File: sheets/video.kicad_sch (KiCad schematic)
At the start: 29 parts, among them U10 74LS273, U11 74LS05, U5 NEO-G0, U6 4364, U7 4364, U80 74HC04, U9 74LS273

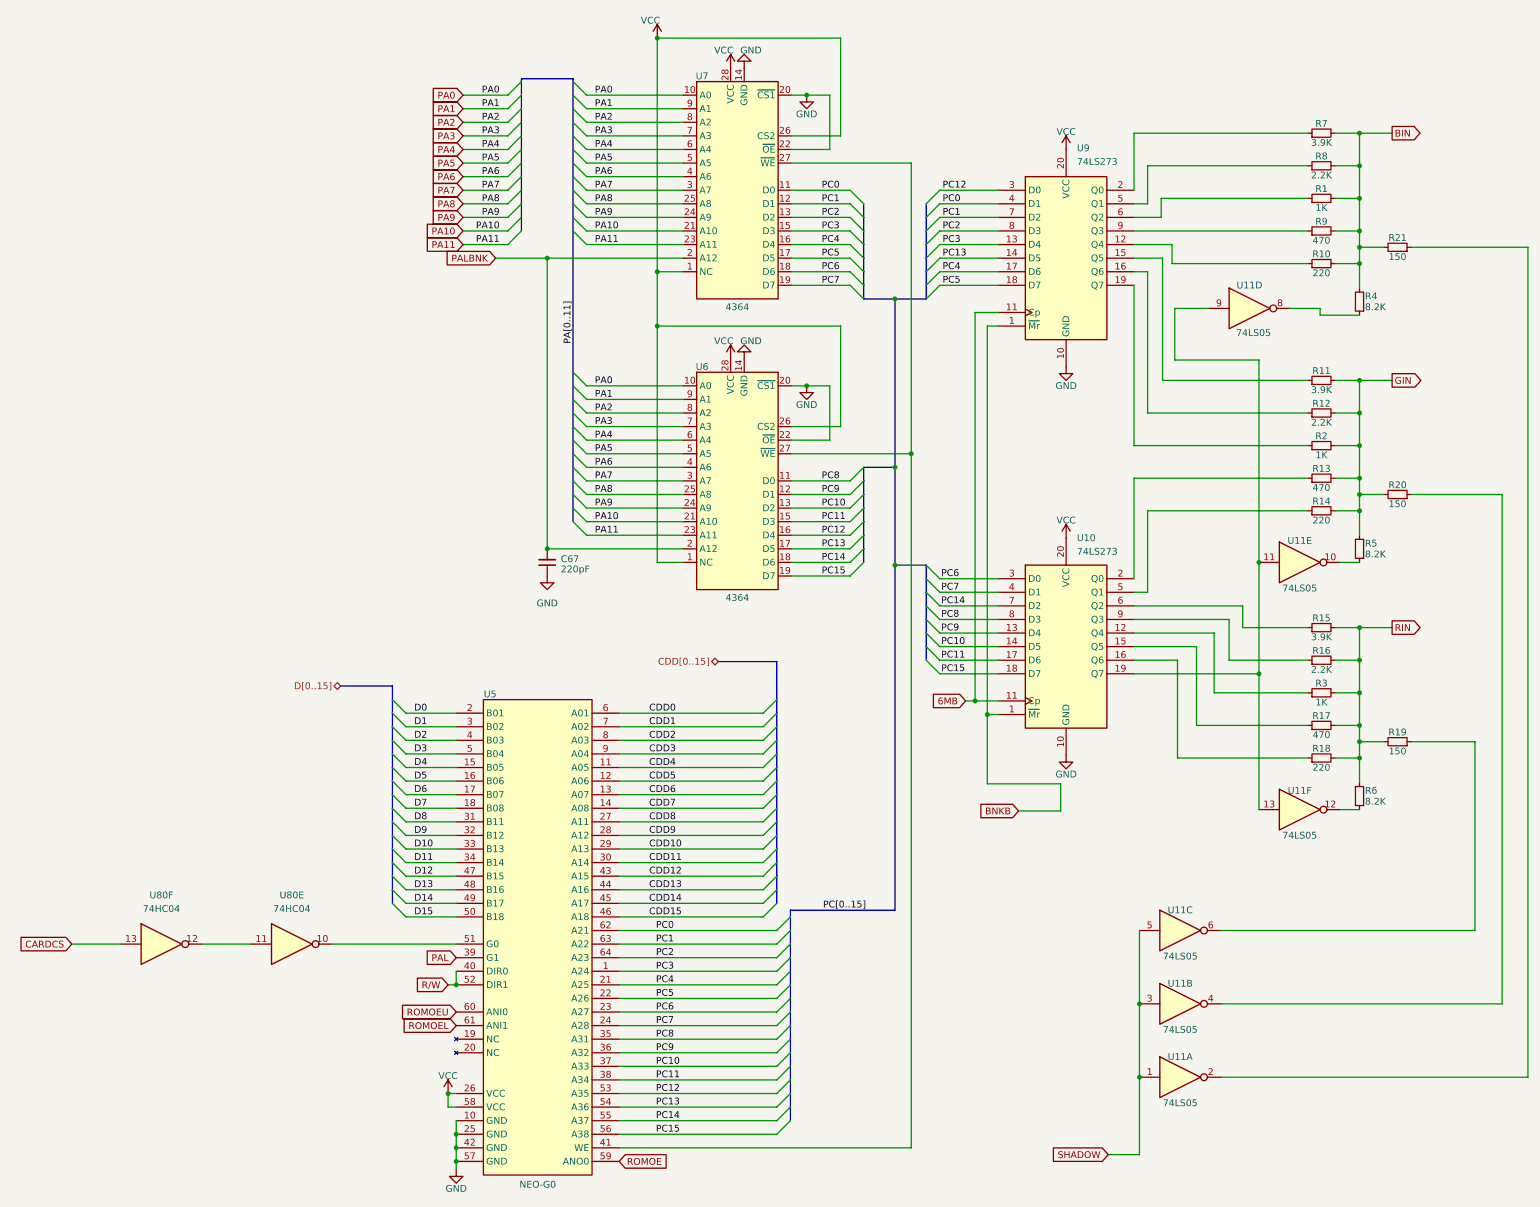
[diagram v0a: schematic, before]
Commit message: Updated to Kicad 10
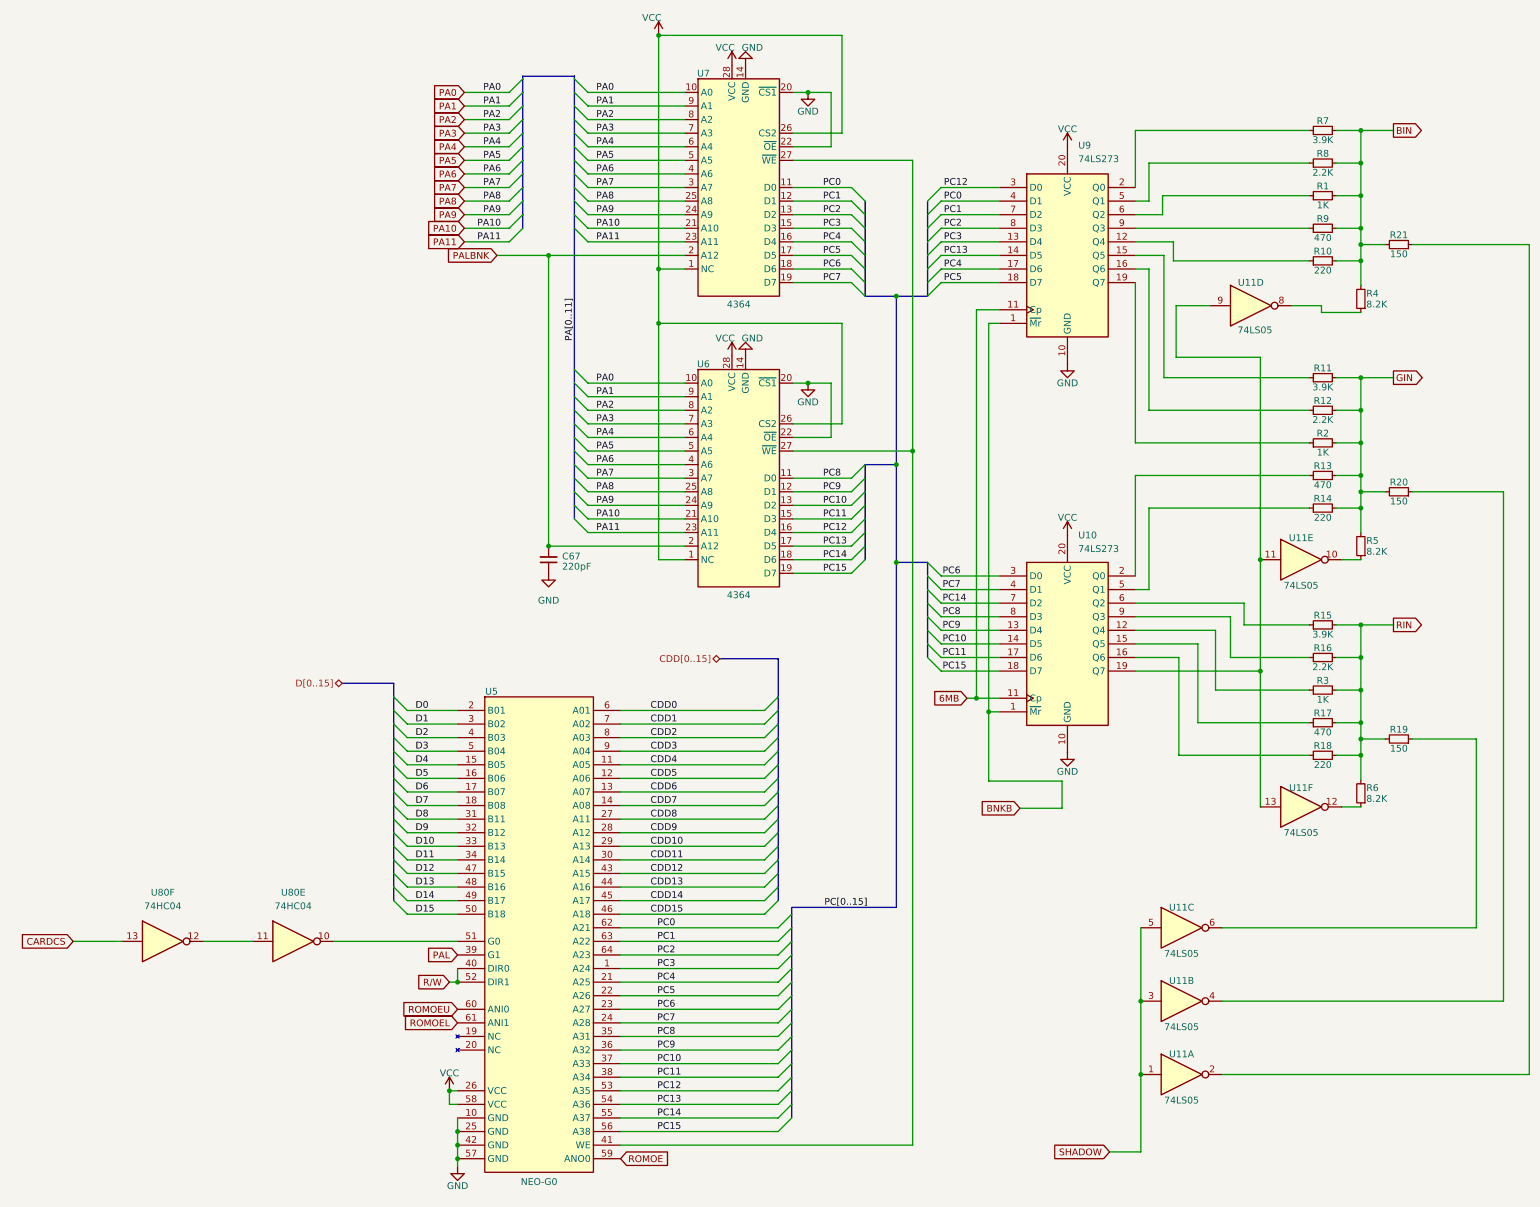
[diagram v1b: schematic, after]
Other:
- moved on the sheet: C67, R1, R10, R11, R12, R13, R14, R15, R16, R17, R18, R19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
